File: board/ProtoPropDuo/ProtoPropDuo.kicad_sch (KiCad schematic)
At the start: 126 parts, among them J1 Conn_01x04, J10 Conn_01x01, J100 Conn_01x01, J101 Conn_01x01, J102 Conn_01x01, J103 Conn_01x01, J104 Conn_01x01, J105 Conn_01x01, J106 Conn_01x01, J107 Conn_01x01, J108 Conn_01x01, J109 Conn_01x01, J11 Conn_01x01, J110 Conn_01x01, J111 Conn_01x01, J112 Conn_01x01, J113 Conn_01x01, J114 Conn_01x01, J115 Conn_01x01, J116 Conn_01x01, J117 Conn_01x01, J118 Conn_01x01, J12 Conn_01x01, J13 Conn_01x01, J14 Conn_01x01, J15 Conn_01x01, J16 Conn_01x01, J17 Conn_01x01, J18 Conn_01x01, J19 Conn_01x01, J2 Conn_01x07, J20 Conn_01x01, J21 Conn_01x01, J22 Conn_01x01, J23 Conn_01x01, J24 Conn_01x01, J25 Conn_01x01, J26 Conn_01x01, J27 Conn_01x01, J28 Conn_01x01, J29 Conn_01x01, J3 Conn_01x20, J30 Conn_01x01, J31 Conn_01x01, J32 Conn_01x01, J33 Conn_01x01, J34 Conn_01x01, J35 Conn_01x01, J36 Conn_01x01, J37 Conn_01x01, J38 Conn_01x01, J39 Conn_01x01, J4 Conn_01x20, J40 Conn_01x01, J41 Conn_01x01, J42 Conn_01x01, J43 Conn_01x01, J44 Conn_01x01, J45 Conn_01x01, J46 Conn_01x01, J47 Conn_01x01, J48 Conn_01x01, J49 Conn_01x01, J5 Conn_01x16, J50 Conn_01x01, J51 Conn_01x01, J52 Conn_01x01, J53 Conn_01x01, J54 Conn_01x01, J55 Conn_01x01, J56 Conn_01x01, J57 Conn_01x01, J58 Conn_01x01, J59 Conn_01x01, J6 Conn_01x12, J60 Conn_01x01, J61 Conn_01x01, J62 Conn_01x01, J63 Conn_01x01, J64 Conn_01x01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

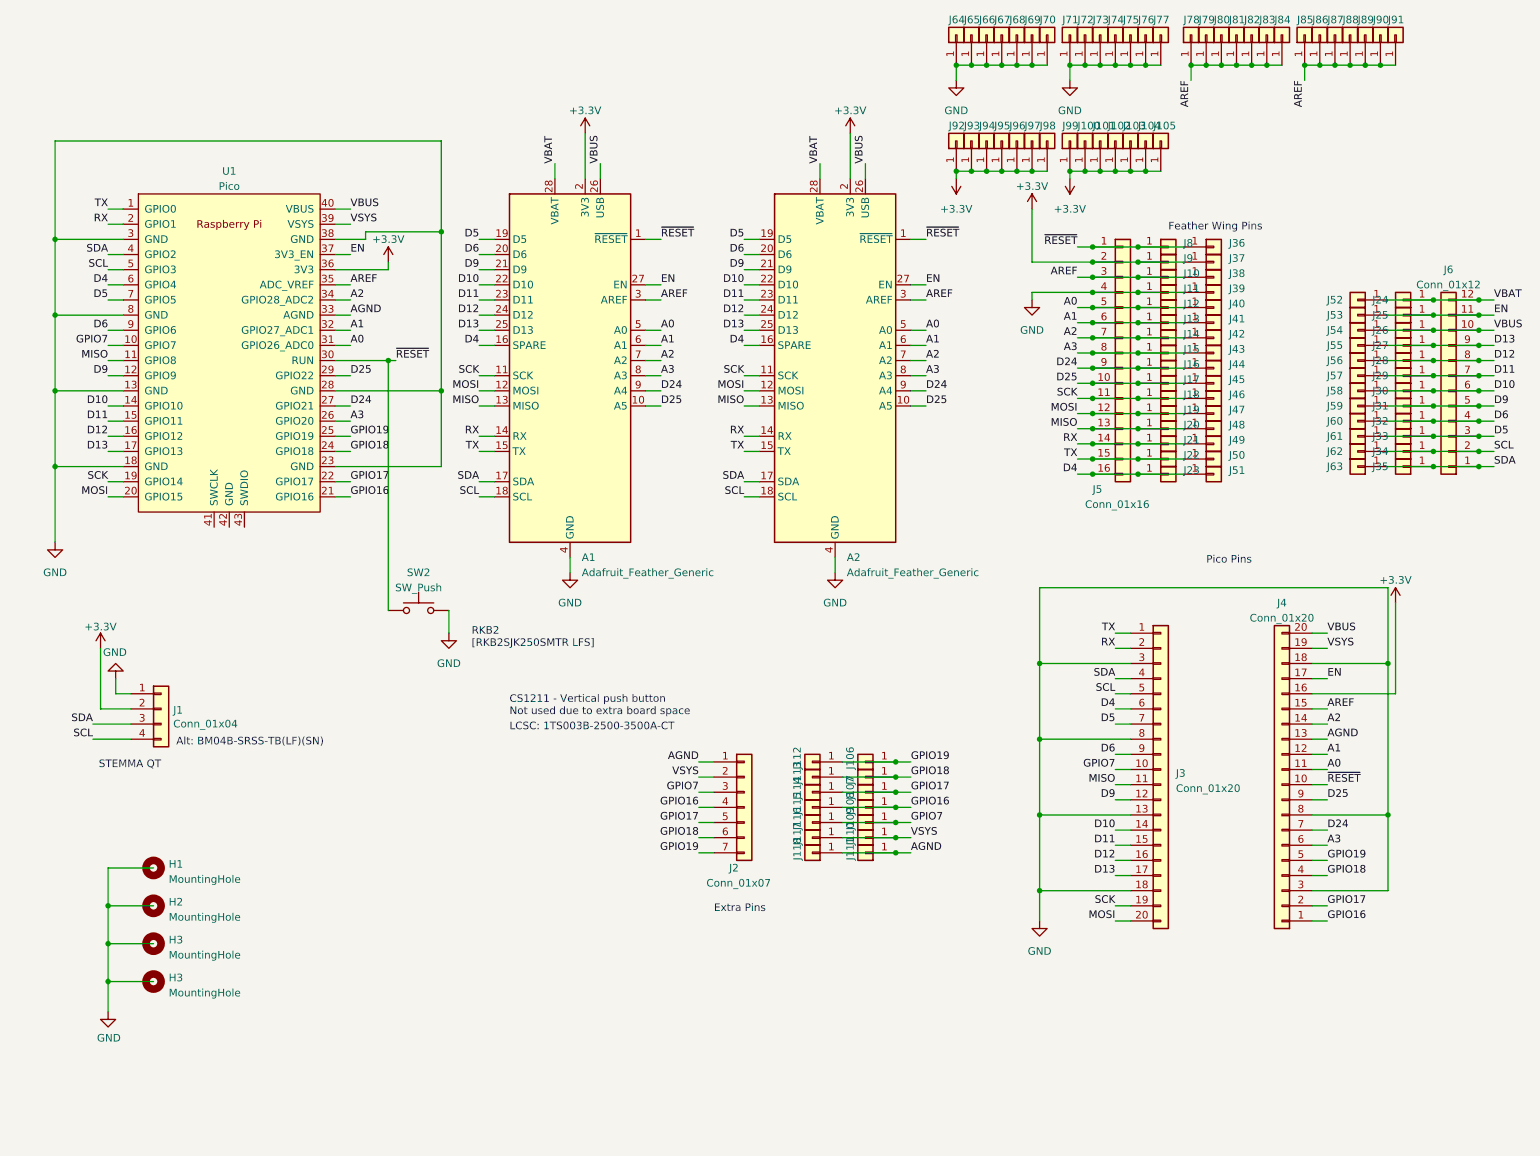
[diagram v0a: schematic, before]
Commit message: Rev B: Reworked the mapping from Pico to featherwing to align some pins for PIO and pwm channels. Added level shifter to support ws2812b individually addressable RGB lights and support for and external 5V power for servos on the extra Pico pins.
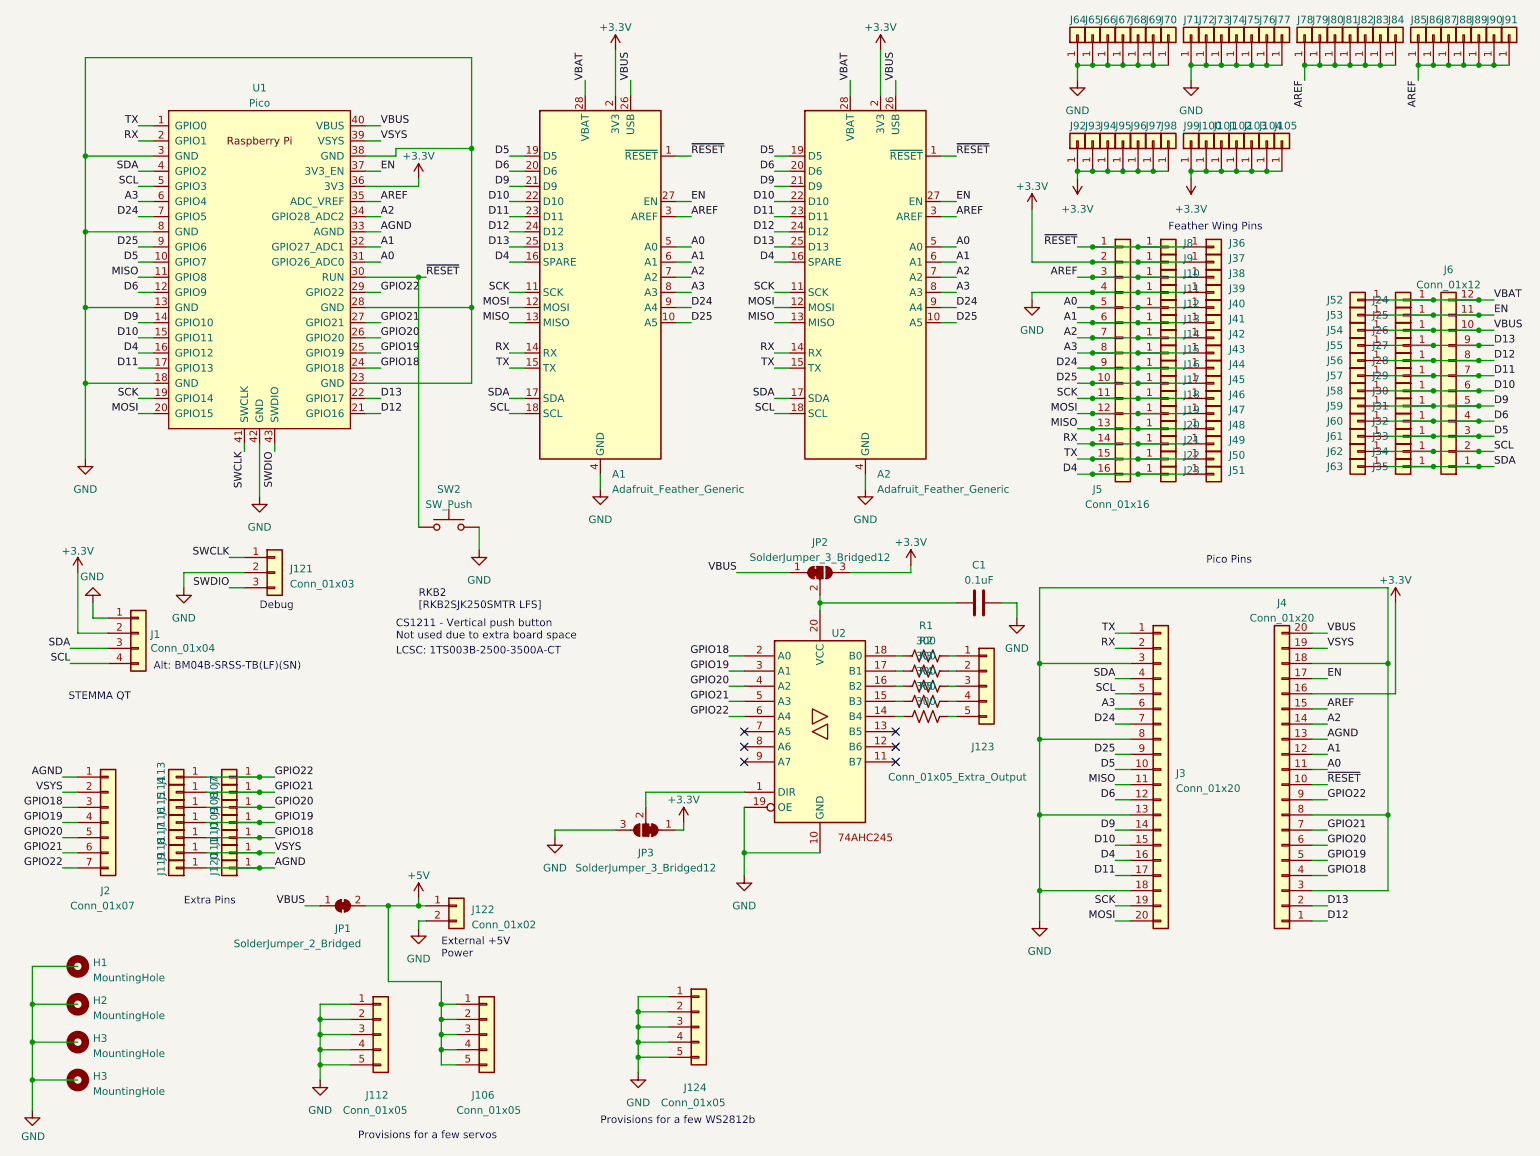
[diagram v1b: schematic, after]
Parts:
- removed J106, J112: Conn_01x01, Department of Alchemy:Grid Hole, symbol Connector_Generic:Conn_01x01
- added C1: 0.1uF, Capacitor_SMD:C_0603_1608Metric_Pad1.08x0.95mm_HandSolder, symbol Device:C
- added J106, J112, J124: Conn_01x05, Connector_PinHeader_2.54mm:PinHeader_1x05_P2.54mm_Vertical, symbol Connector_Generic:Conn_01x05
- added J119, J120: Conn_01x01, Department of Alchemy:Grid Hole, symbol Connector_Generic:Conn_01x01
- added J121: Conn_01x03, Connector_PinHeader_2.54mm:PinHeader_1x03_P2.54mm_Vertical, symbol Connector_Generic:Conn_01x03
- added J122: Conn_01x02, Connector_PinHeader_2.54mm:PinHeader_1x02_P2.54mm_Vertical, symbol Connector_Generic:Conn_01x02
- added J123: Conn_01x05_Extra_Output, Connector_PinHeader_2.54mm:PinHeader_1x05_P2.54mm_Vertical, symbol Connector_Generic:Conn_01x05
- added JP1: SolderJumper_2_Bridged, Jumper:SolderJumper-2_P1.3mm_Bridged_Pad1.0x1.5mm, symbol Jumper:SolderJumper_2_Bridged
- added JP2, JP3: SolderJumper_3_Bridged12, Jumper:SolderJumper-3_P1.3mm_Bridged12_Pad1.0x1.5mm, symbol Jumper:SolderJumper_3_Bridged12
- added R1, R2, R3, R4, R5: 300, Resistor_SMD:R_0603_1608Metric_Pad0.98x0.95mm_HandSolder, symbol Device:R_US
- added U2: ~, Department of Alchemy:SOP65P640X120-20N, symbol Department of Alchemy:74AHC245
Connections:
- net +3.3V: now also JP2.3 (B), JP3.1 (A)
- net A3: now also J3.6 (Pin_6), U1.6 (GPIO4); no longer J4.6 (Pin_6), U1.26 (GPIO20)
- net AGND: now also J119.1 (Pin_1), J120.1 (Pin_1); no longer J111.1 (Pin_1), J118.1 (Pin_1)
- net D10: now also J3.15 (Pin_15), U1.15 (GPIO11); no longer J3.14 (Pin_14), U1.14 (GPIO10)
- net D11: now also J3.17 (Pin_17), U1.17 (GPIO13); no longer J3.15 (Pin_15), U1.15 (GPIO11)
- net D12: now also J4.1 (Pin_1), U1.21 (GPIO16); no longer J3.16 (Pin_16), U1.16 (GPIO12)
- net D13: now also J4.2 (Pin_2), U1.22 (GPIO17); no longer J3.17 (Pin_17), U1.17 (GPIO13)
- net D24: now also J3.7 (Pin_7), U1.7 (GPIO5); no longer J4.7 (Pin_7), U1.27 (GPIO21)
- net D25: now also J3.9 (Pin_9), U1.9 (GPIO6); no longer J4.9 (Pin_9), U1.29 (GPIO22)
- net D4: now also J3.16 (Pin_16), U1.16 (GPIO12); no longer J3.6 (Pin_6), U1.6 (GPIO4)
- net D5: now also J3.10 (Pin_10), U1.10 (GPIO7); no longer J3.7 (Pin_7), U1.7 (GPIO5)
- net D6: now also J3.12 (Pin_12), U1.12 (GPIO9); no longer J3.9 (Pin_9), U1.9 (GPIO6)
- net D9: now also J3.14 (Pin_14), U1.14 (GPIO10); no longer J3.12 (Pin_12), U1.12 (GPIO9)
- net GND: now also U1.42 (GND), C1.2, J112.1 (Pin_1), J112.2 (Pin_2), J112.3 (Pin_3), J112.4 (Pin_4), J112.5 (Pin_5), J121.2 (Pin_2), J122.2 (Pin_2), J124.1 (Pin_1), J124.2 (Pin_2), J124.3 (Pin_3), J124.4 (Pin_4), J124.5 (Pin_5), JP3.3 (B), U2.10 (GND), U2.19 (OE)
- net GPIO18: now also J110.1 (Pin_1), J117.1 (Pin_1), J2.3 (Pin_3), U2.2 (A0); no longer J113.1 (Pin_1), J2.6 (Pin_6), J7.1 (Pin_1)
- net GPIO19: now also J109.1 (Pin_1), J116.1 (Pin_1), J2.4 (Pin_4), U2.3 (A1); no longer J2.7 (Pin_7)
- net VBUS: now also JP1.1 (A), JP2.1 (A)
- net VSYS: now also J111.1 (Pin_1), J118.1 (Pin_1); no longer J110.1 (Pin_1), J117.1 (Pin_1)
- net SWCLK: now reaches U1.41 (SWCLK)
- net SWCLK: now also J121.1 (Pin_1)
- net SWDIO: now reaches U1.43 (SWDIO)
- net SWDIO: now also J121.3 (Pin_3)
- removed net GPIO16: J108.1 (Pin_1), J115.1 (Pin_1), J2.4 (Pin_4), J4.1 (Pin_1), U1.21 (GPIO16)
- removed net GPIO17: J107.1 (Pin_1), J114.1 (Pin_1), J2.5 (Pin_5), J4.2 (Pin_2), U1.22 (GPIO17)
- removed net GPIO7: J109.1 (Pin_1), J116.1 (Pin_1), J2.3 (Pin_3), J3.10 (Pin_10), U1.10 (GPIO7)
- new net: R1.1, U2.18 (B0)
- new net: J123.1 (Pin_1), R1.2
- new net: R2.1, U2.17 (B1)
- new net: J123.2 (Pin_2), R2.2
- new net: R5.1, U2.14 (B4)
- new net: J123.5 (Pin_5), R5.2
- new net: R3.1, U2.16 (B2)
- new net: J123.3 (Pin_3), R3.2
- new net: J123.4 (Pin_4), R4.2
- new net: C1.1, JP2.2 (C), U2.20 (VCC)
- new net: R4.1, U2.15 (B3)
- new net: JP3.2 (C), U2.1 (DIR)
- new net +5V: J106.1 (Pin_1), J106.2 (Pin_2), J106.3 (Pin_3), J106.4 (Pin_4), J106.5 (Pin_5), J122.1 (Pin_1), JP1.2 (B)
- new net GPIO20: J108.1 (Pin_1), J115.1 (Pin_1), J2.5 (Pin_5), J4.6 (Pin_6), U1.26 (GPIO20), U2.4 (A2)
- new net GPIO21: J107.1 (Pin_1), J114.1 (Pin_1), J2.6 (Pin_6), J4.7 (Pin_7), U1.27 (GPIO21), U2.5 (A3)
- new net GPIO22: J113.1 (Pin_1), J2.7 (Pin_7), J4.9 (Pin_9), J7.1 (Pin_1), U1.29 (GPIO22), U2.6 (A4)
- no-connect marks 0 -> 6
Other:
- note added: "Debug"
- note added: "External +5V Power"
- note added: "Provisions for a few WS2812b"
- note added: "Provisions for a few servos"
- title: Raspberry Pi Pico Feather Wing Duo -> Proto Prop Duo
- moved on the sheet: A1, A2, H1, H2, H3, J1, J100, J101, J102, J103, J104, J105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
